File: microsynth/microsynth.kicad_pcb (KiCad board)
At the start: 2 copper layers, 365.8 x 155 mm, 260 parts, among them J1 AudioJack3, J2 Conn_01x03_Male, J3 Conn_01x04_Male, J4 Conn_01x04_Male, J5 Conn_01x02_Male, J8 AudioJack2, Q1 BC182, Q2 BC182L, Q3 BC548, Q4 BC212 PNP, Q5 BC212 PNP, Q6 BC548, Q7 BC548, Q8 BC548, Q9 BC548, SW1 DRIFT, SW10 SW_SPST, SW11 SW_SPDT, SW12 SOURCE, SW13 THUMBWEEL, SW14 SW_SPDT, SW15 SW_SPDT, SW16 SW_SPDT, SW17 SW_SPDT, SW18-ENV-TO-VCF1 SW_SPDT, SW19-ENV-TO-VCO1 SW_SPDT, SW2 RANGE, SW20-ENV-TO-KEYB1 SW_SPDT, SW21 SW_Rotary2x6, SW22 SW_SPST, SW3 SW_DPTT_SELECTOR, SW4 SW_DPTT_SELECTOR, SW5 SW_SPDT, SW6 SW_DPTT_SELECTOR, SW7 SW_SPDT, SW8 SW_DPTT_SELECTOR-Switch, SW9 TRIGGER, U1 RC4136, U10 LM741, U11 LM741, U12 LM741, U13 LM741, U14 4016, U15 LF355, U16 LM741, U17 LM741, U18 LM741, U19 LM741, U2 TL072, U20 LM13600, U21 CA3080, U22 4013, U23 LM380N, U3 4011, U4 4016, U5 LF347, U6 TL071, U7 LM741, U8 4001, U9 LM741

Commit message: Layout...
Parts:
- moved R99 29.0 mm to (247.4, 226.8)
- moved R105 16.5 mm to (333.8, 141.0), turned to 270 degrees
- moved R84 9.46 mm to (208.5, 98.4)
- moved R142 6.89 mm to (344.1, 223.5), turned to 270 degrees
- moved R86 0.13 mm to (218.7, 101.5)
- turned SW16 to 270 degrees
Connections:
- C30 pad 1: LFO_MOD -> LFO_MOD_S17
- R99 pad 2: LFO_MOD -> LFO_MOD_S16
- SW16 pad 1: LFO_MOD -> LFO_MOD_S16
- SW17 pad 1: LFO_MOD -> LFO_MOD_S17
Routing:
- net Net-(R142-Pad2): track 76.3 -> 328.4 mm, vias 0 -> 1
- net VCO1_SAW1: track 10.3 -> 205.1 mm
- net Net-(D8-Pad1): track 80.2 -> 196.4 mm, vias 0 -> 1
- net VCO2_MOD_SWITCH_S6-1: track 0.00 -> 110.9 mm, vias 0 -> 1
- net TO_VCA_C27: track 142.0 -> 231.7 mm, vias 2 -> 3
- net Net-(C12-Pad1): track 15.1 -> 103.9 mm, vias 0 -> 2
- net KEYBOARD_IC7_PIN_6: track 109.6 -> 193.4 mm
- net LFO_MOD: track 76.2 -> 0.00 mm
- net GND: track 943.5 -> 1015.2 mm
- net -15V: track 1231.7 -> 1282.8 mm
- net LFO_TO_VR20_SLIDER: track 185.8 -> 211.6 mm
- net LFO_MOD_S17: track 0.00 -> 22.2 mm
- net TO_VCA_C26: track 302.4 -> 318.4 mm
- net TO_VCF_IC20_3: track 377.4 -> 393.1 mm
- net IC22_PIN_3: track 190.1 -> 180.5 mm
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
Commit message: Layout...
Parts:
- SW1: footprint Buttons_Switches_ThroughHole:OS203013MT8QN1 -> Buttons_Switches_ThroughHole:L203011MS02Q
- SW12, SW13: footprint Buttons_Switches_ThroughHole:DP3T_Toggle -> Buttons_Switches_ThroughHole:L203011MS02Q
- moved R140 7.33 mm to (104.7, 222.4)
- moved R31 3.91 mm to (36.7, 225.6)
- moved SW4 1.42 mm to (121.9, 201.3)
- moved SW12 1.27 mm to (86.4, 223.5)
- moved SW13 1.27 mm to (121.9, 223.5)
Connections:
- SW12 pad 1: (no net) -> Net-(D10-Pad2)
- SW12 pad 5: Net-(D10-Pad2) -> (no net)
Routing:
- net TO_IC5_PIN7: track 2.54 -> 195.6 mm
- net VCO1_SAW1: track 205.1 -> 381.3 mm, vias 0 -> 1
- net S5_VCO2: track 46.9 -> 112.3 mm, vias 0 -> 2
- net IC22_PIN_3: track 180.5 -> 197.6 mm, vias 0 -> 1
- net Net-(RV27-Pad3): track 64.4 -> 78.0 mm, vias 0 -> 1
- net Net-(RV27-Pad2): track 97.1 -> 109.7 mm
- net +15V: track 1265.0 -> 1271.8 mm
- net THUMBWEEL_MOD: track 85.8 -> 80.7 mm
- net THUMBWEEL_MOD_TO_S13: track 66.8 -> 71.5 mm
- net GND: track 1015.2 -> 1019.3 mm
- net ENVELOPE: track 176.8 -> 180.8 mm
- net Net-(C12-Pad1): track 103.9 -> 107.5 mm
- net TO_KBD_R140: track 7.50 -> 11.0 mm
- net Net-(D10-Pad2): track 40.4 -> 37.0 mm
- net LFO_TO_VR20_SLIDER: track 211.6 -> 209.1 mm
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
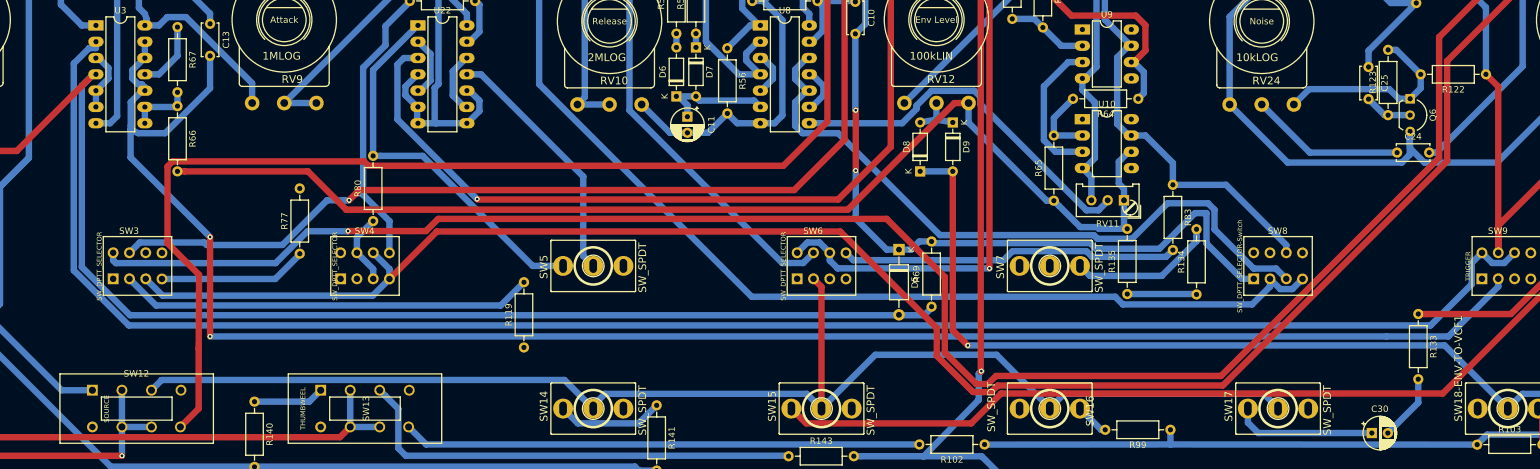
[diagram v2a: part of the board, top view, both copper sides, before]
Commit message: Add 3d models
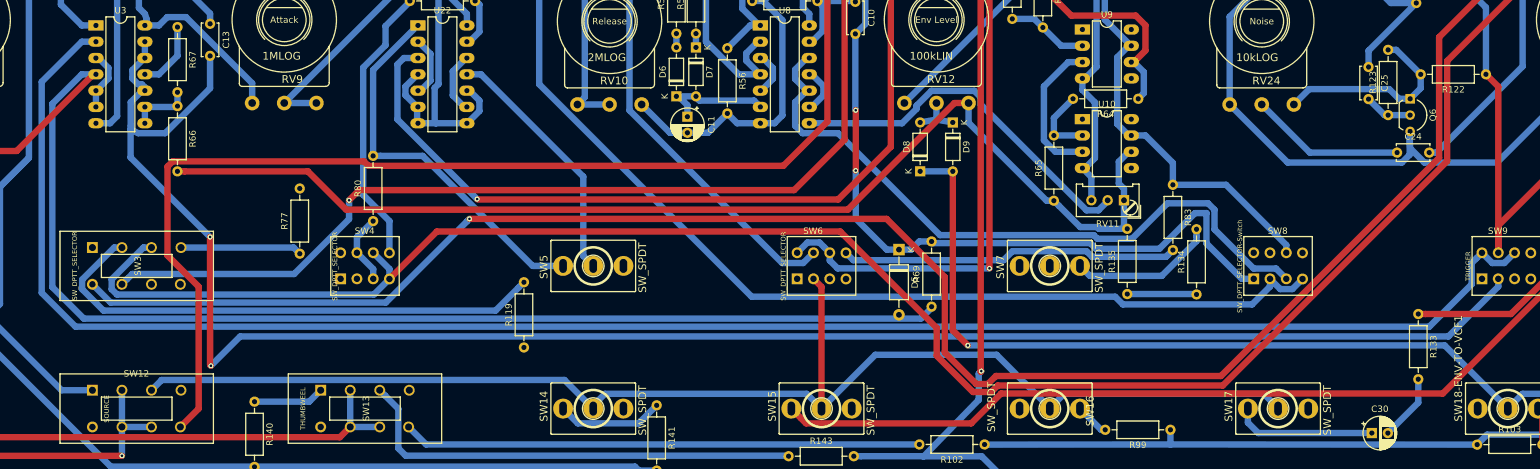
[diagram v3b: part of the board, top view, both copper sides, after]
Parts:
- SW3: footprint Buttons_Switches_ThroughHole:DP3T_Toggle -> Buttons_Switches_ThroughHole:L203011MS02Q
- moved SW3 1.14 mm to (86.4, 201.3)
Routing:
- net VCO1_SAW2: track 64.7 -> 81.8 mm
- net TO_VCF_IC20_3: track 393.9 -> 408.2 mm
- net Net-(SW9-Pad5): track 273.6 -> 283.6 mm
- net TO_D4: track 202.6 -> 212.4 mm
- net Net-(C13-Pad2): track 279.7 -> 286.1 mm
- net TO_VCA_C26: track 320.1 -> 325.6 mm
- net VCO1_SAW1: track 381.3 -> 385.9 mm
- net VCO1_SQR: track 23.1 -> 18.9 mm

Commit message: Change switch footprints
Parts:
- SW4, SW6, SW8, SW9: footprint Buttons_Switches_ThroughHole:DP3T_Toggle -> Buttons_Switches_ThroughHole:L203011MS02Q
- moved R77 7.34 mm to (104.5, 198.7)
- moved R83 3.11 mm to (244.8, 189.5)
- moved R134 1.84 mm to (249.6, 205.7)
- moved D5 1.71 mm to (206.8, 198.8)
- moved SW9 1.27 mm to (299.7, 201.3)
- moved SW6 1.27 mm to (193.0, 201.3)
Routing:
- net Net-(R77-Pad2): track 0.00 -> 419.4 mm
- net Net-(C17-Pad1): track 65.2 -> 251.5 mm, vias 0 -> 1
- net KEYBOARD_IC7_PIN_6: track 193.4 -> 109.6 mm
- net Net-(SW21-Pad14): track 0.00 -> 76.4 mm
- net GND: track 1019.3 -> 1091.3 mm, vias 2 -> 3
- net +15V: track 1271.8 -> 1343.1 mm
- net HOLD_ON: track 0.00 -> 55.2 mm
- net Net-(R133-Pad1): track 101.3 -> 143.0 mm, vias 1 -> 2
- net LFO_TO_VR20_SLIDER: track 209.1 -> 223.5 mm
- net TO_VCA_C26: track 325.6 -> 339.3 mm
- net Net-(C10-Pad2): track 119.5 -> 111.0 mm
- net TO_VCF_IC20_3: track 408.2 -> 416.6 mm
- net VCO1_SQR: track 18.9 -> 11.3 mm
- net Net-(R61-Pad2): track 200.2 -> 206.8 mm
- net Net-(R81-Pad1): track 44.0 -> 50.1 mm
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
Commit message: Layout...-11
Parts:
- RV11, RV19, RV22, RV3, RV4, RV5, RV6, RV7: moved to B.Cu
- moved RV3 0.06 mm to (121.5, 130.4)
- moved RV4 0.06 mm to (77.5, 109.9), turned to 180 degrees
- turned RV7 to 270 degrees
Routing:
- net S5_VCO2: track 112.3 -> 218.2 mm, vias 2 -> 3
- net +15V: track 1343.1 -> 1438.6 mm
- net LFO_TO_VR20_SLIDER: track 223.5 -> 313.3 mm
- net Net-(SW21-Pad14): track 76.4 -> 0.00 mm
- net Net-(C11-Pad1): track 17.1 -> 76.1 mm, vias 0 -> 2
- net -15V: track 1281.4 -> 1297.0 mm
- net TO_IC5_PIN7: track 195.6 -> 208.6 mm
- net Net-(C31-Pad2): track 18.7 -> 29.3 mm
- net VCO2_SAW: track 104.8 -> 110.5 mm
- net Net-(C20-Pad2): track 66.2 -> 71.0 mm
- net VCO1_SAW1: track 384.2 -> 388.3 mm
- net GND: track 1091.3 -> 1092.7 mm

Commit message: Layout...-7
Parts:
- RV13, RV15, RV17, RV8: moved to B.Cu
- moved R150 22.8 mm to (310.0, 143.6), turned to 0 degrees
- moved R134 4.26 mm to (249.4, 210.0)
- moved R119 3.24 mm to (146.7, 217.2)
- moved RV8 0.18 mm to (137.8, 116.2)
- moved R93 0.10 mm to (271.5, 90.6)
- moved RV13 0.06 mm to (189.3, 111.8)
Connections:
- SW8 pad 1: Net-(C10-Pad2) -> (no net)
- SW8 pad 2: Net-(R61-Pad2) -> (no net)
- SW8 pad 3: Net-(SW8-Pad3) -> +15V
- SW8 pad 4: Net-(R61-Pad2) -> HOLD_ON
- SW8 pad 5: (no net) -> Net-(C10-Pad2)
- SW8 pad 6: (no net) -> Net-(R61-Pad2)
- SW8 pad 7: +15V -> Net-(SW8-Pad7)
- SW8 pad 8: HOLD_ON -> Net-(R61-Pad2)
- U8 pad 10: Net-(SW8-Pad3) -> Net-(SW8-Pad7)
- U8 pad 12: Net-(SW8-Pad3) -> Net-(SW8-Pad7)
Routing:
- net KEYBOARD_IC7_PIN_6: track 109.6 -> 422.2 mm, vias 0 -> 2
- net Net-(C7-Pad1): track 32.4 -> 287.2 mm
- net Net-(R150-Pad1): track 0.00 -> 176.7 mm
- net Net-(SW8-Pad7): track 0.00 -> 106.5 mm
- net Net-(SW8-Pad3): track 103.6 -> 0.00 mm
- net S5_VCO2: track 218.2 -> 319.2 mm
- net GND: track 1092.7 -> 1103.7 mm
- net HOLD_ON: track 55.2 -> 64.9 mm
- net -15V: track 1297.0 -> 1303.7 mm, vias 8 -> 10
- net Net-(C10-Pad2): track 111.0 -> 116.5 mm
- net Net-(C17-Pad1): track 251.5 -> 256.1 mm, vias 1 -> 2
- net TO_VCA_C26: track 339.3 -> 343.8 mm
- net ADSR: track 21.7 -> 17.4 mm
- net Net-(R133-Pad1): track 143.0 -> 146.0 mm
- net Net-(R72-Pad1): track 93.8 -> 96.7 mm
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
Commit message: Layout...-3
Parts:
- J1: footprint 4ms_Jack:EighthInch_Stereo_PJ366ST_ALT -> Connector_PinHeader_2.54mm:PinHeader_1x03_P2.54mm_Vertical; moved to B.Cu
- J2: moved to B.Cu
- J8: footprint 4ms_Jack:EighthInch_Stereo_PJ366ST_ALT -> Connector_PinHeader_2.54mm:PinHeader_1x02_P2.54mm_Vertical; moved to B.Cu
- RV26: footprint 4ms_Potentiometer:Pot_16mm_NoDet_RV16AF-4A -> Connector_PinHeader_2.54mm:PinHeader_1x03_P2.54mm_Vertical; moved to B.Cu
- SW8: value SW_DPTT_SELECTOR-Switch -> SUSTAIN
- moved J8 15.0 mm to (377.9, 95.2), turned to 270 degrees
- moved RV26 13.3 mm to (361.7, 95.4), turned to 270 degrees
- moved R136 7.33 mm to (307.0, 191.5), turned to 180 degrees
- moved J1 5.11 mm to (389.2, 95.2), turned to 90 degrees
- moved C31 3.30 mm to (373.0, 94.6)
- moved C10 2.86 mm to (195.5, 160.1)
- turned J2 to 270 degrees
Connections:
- R136 pad 2: HOLD_ON -> TO_VCA_R136
- R145 pad 2: Net-(J1-PadR) -> Net-(J1-Pad2)
- R146 pad 1: Net-(J1-PadS) -> Net-(J1-Pad1)
- SW8 pad 1: (no net) -> Net-(C10-Pad2)
- SW8 pad 2: (no net) -> Net-(R61-Pad2)
- SW8 pad 3: +15V -> Net-(SW8-Pad3)
- SW8 pad 4: HOLD_ON -> Net-(R61-Pad2)
- SW8 pad 5: Net-(C10-Pad2) -> (no net)
- SW8 pad 6: Net-(R61-Pad2) -> (no net)
- SW8 pad 7: Net-(SW8-Pad7) -> +15V
- SW8 pad 8: Net-(R61-Pad2) -> TO_VCA_R136
- SW9 pad 1: (no net) -> Net-(SW9-Pad1)
- SW9 pad 2: Net-(C13-Pad2) -> +15V
- SW9 pad 3: TO_D3 -> Net-(SW9-Pad1)
- SW9 pad 4: (no net) -> S5_VCO2
- SW9 pad 5: Net-(SW9-Pad5) -> (no net)
- SW9 pad 6: +15V -> TO_D3
- SW9 pad 7: Net-(SW9-Pad5) -> Net-(C13-Pad2)
- SW9 pad 8: S5_VCO2 -> (no net)
- U3 pad 2: Net-(SW9-Pad5) -> Net-(SW9-Pad1)
- U8 pad 10: Net-(SW8-Pad7) -> Net-(SW8-Pad3)
- U8 pad 12: Net-(SW8-Pad7) -> Net-(SW8-Pad3)
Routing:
- net Net-(SW9-Pad1): track 0.00 -> 293.7 mm
- net Net-(SW9-Pad5): track 283.1 -> 0.00 mm
- net LFO_TO_VR20_SLIDER: track 312.7 -> 499.7 mm
- net Net-(R133-Pad1): track 146.0 -> 317.0 mm, vias 2 -> 3
- net TO_D3: track 203.7 -> 345.7 mm, vias 1 -> 3
- net Net-(SW8-Pad7): track 106.5 -> 0.00 mm
- net Net-(SW8-Pad3): track 0.00 -> 100.4 mm
- net Net-(R139-Pad2): track 0.00 -> 99.4 mm, vias 0 -> 1
- net HOLD_ON: track 64.9 -> 0.00 mm
- net TO_VCA_R136: track 0.00 -> 31.1 mm
- net Net-(R77-Pad2): track 420.6 -> 405.5 mm
- net Net-(C31-Pad2): track 29.3 -> 17.6 mm
- net Net-(J1-Pad1): track 0.00 -> 10.7 mm
- net Net-(J1-Pad2): track 0.00 -> 10.7 mm
- net Net-(C10-Pad2): track 116.5 -> 106.4 mm
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
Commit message: Move connectors to back
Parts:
- J4, RV25: moved to B.Cu
- moved J4 0.46 mm to (29.6, 151.1), turned to 0 degrees
